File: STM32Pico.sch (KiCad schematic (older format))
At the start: 25 parts, among them J1 2.54mm header 01x20, J2 2.54mm header 01x20, SW1 Boot Mode, SW2 Reset Switch, U1 STM32F411CEUx, U2 XC6206PxxxMR, X1 ECS-2520MV-xxx-xx

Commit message: finished up board design, likely needs some check overs and revision.
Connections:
- net GND: now also U1.23 (VSS), U1.35 (VSS), U1.47 (VSS)
- net PA0: now also J1.4 (Pin_4)
- net PA1: now also J1.2 (Pin_2)
- net PA10: now also J2.6 (Pin_6)
- net PA13: now also J1.20 (Pin_20)
- net PA14: now also J1.19 (Pin_19)
- net PA15: now also J1.17 (Pin_17)
- net PA2: now also J1.1 (Pin_1)
- net PA7: now also J2.20 (Pin_20)
- net PA8: now also J2.9 (Pin_9)
- net PA9: now also J2.7 (Pin_7)
- net PB0: now also J2.19 (Pin_19)
- net PB1: now also J2.17 (Pin_17)
- net PB10: now also J2.15 (Pin_15)
- net PB12: now also J2.14 (Pin_14)
- net PB13: now also J2.12 (Pin_12)
- net PB14: now also J2.11 (Pin_11)
- net PB15: now also J2.10 (Pin_10)
- net PB2: now also J2.16 (Pin_16)
- net PB3: now also J1.16 (Pin_16)
- net PB4: now also J1.15 (Pin_15)
- net PB5: now also J1.14 (Pin_14)
- net PB6: now also J1.12 (Pin_12)
- net PB7: now also J1.11 (Pin_11)
- net PB8: now also J1.10 (Pin_10)
- net PB9: now also J1.9 (Pin_9)
- net PC15: now reaches J1.5 (Pin_5)
- net PC15: now also U1.4 (PC15)
- net PC14: now reaches J1.6 (Pin_6)
- net PC14: now also U1.3 (PC14)
- net PC13: now reaches J1.7 (Pin_7)
- net PC13: now also U1.2 (PC13)
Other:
- moved on the sheet: J1, J2

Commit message: properly seperated VBUS and VSYS however VSYS is now 5V output only since its not connected to the power management IC
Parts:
- D1: value Schottky 0603 -> 1N4002 0603; symbol Device:D_Schottky -> Device:D
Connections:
- net VBUS: no longer D1.1 (K), J2.2 (Pin_2)
- new net VSYS: D1.1 (K), J2.2 (Pin_2)
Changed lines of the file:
@@
-$EndComp
-$Comp
-L power:VBUS #PWR016
-U 1 1 615E9702
-P 3200 1500
-F 0 "#PWR016" H 3200 1350 50  0001 C CNN
-F 1 "VBUS" V 3215 1627 50  0000 L CNN
-F 2 "" H 3200 1500 50  0001 C CNN
-F 3 "" H 3200 1500 50  0001 C CNN
-	1    3200 1500
-	0    -1   -1   0
 $EndComp
 $Comp
@@
 	6150 7250 6450 7250
 $Comp
-L Device:D_Schottky D1
+L Device:D D1
 U 1 1 611CF5D5
 P 3350 1500
 F 0 "D1" H 3350 1331 50  0000 C CNN
-F 1 "Schottky 0603" H 3350 1398 20  0000 C CNN
+F 1 "1N4002 0603" H 3350 1398 20  0000 C CNN
 F 2 "Diode_SMD:D_0603_1608Metric" H 3350 1500 50  0001 C CNN
 F 3 "~" H 3350 1500 50  0001 C CNN
@@
 	3650 1950 3800 1950
 Connection ~ 3800 1950
-$Comp
-L VSYS:VSYS #PWR0101
-U 1 1 610575B5
-P 3650 1950
-F 0 "#PWR0101" H 3650 1800 50  0001 C CNN
-F 1 "VSYS" V 3665 2077 50  0000 L CNN
-F 2 "" H 3650 1950 50  0001 C CNN
-F 3 "" H 3650 1950 50  0001 C CNN
-	1    3650 1950
-	0    -1   -1   0
-$EndComp
-$Comp
-L VSYS:VSYS #PWR0102
-U 1 1 61057CA3
-P 3500 1500
-F 0 "#PWR0102" H 3500 1350 50  0001 C CNN
-F 1 "VSYS" V 3515 1628 50  0000 L CNN
-F 2 "" H 3500 1500 50  0001 C CNN
-F 3 "" H 3500 1500 50  0001 C CNN
-	1    3500 1500
-	0    1    1    0
-$EndComp
-$Comp
-L VSYS:VSYS #PWR0103
-U 1 1 61058306
-P 6400 7050
-F 0 "#PWR0103" H 6400 6900 50  0001 C CNN
-F 1 "VSYS" V 6415 7177 50  0000 L CNN
-F 2 "" H 6400 7050 50  0001 C CNN
-F 3 "" H 6400 7050 50  0001 C CNN
-	1    6400 7050
-	0    -1   -1   0
-$EndComp
 Text GLabel 2200 8550 0    50   Input ~ 0
 PB0
@@
 Text GLabel 6450 8850 0    50   Input ~ 0
 PA7
+$Comp
+L power:VBUS #PWR016
+U 1 1 615E9702
+P 3200 1500
+F 0 "#PWR016" H 3200 1350 50  0001 C CNN
+F 1 "VBUS" V 3215 1627 50  0000 L CNN
+F 2 "" H 3200 1500 50  0001 C CNN
+F 3 "" H 3200 1500 50  0001 C CNN
+	1    3200 1500
+	0    -1   -1   0
+$EndComp
+Text GLabel 3500 1500 2    50   Input ~ 0
+VSYS
+$Comp
+L power:VBUS #PWR?
+U 1 1 6117FC90
+P 3650 1950
+F 0 "#PWR?" H 3650 1800 50  0001 C CNN
+F 1 "VBUS" V 3665 2077 50  0000 L CNN
+F 2 "" H 3650 1950 50  0001 C CNN
+F 3 "" H 3650 1950 50  0001 C CNN
+	1    3650 1950
+	0    -1   -1   0
+$EndComp
+Text GLabel 6400 7050 0    50   Input ~ 0
+VSYS
 $EndSCHEMATC

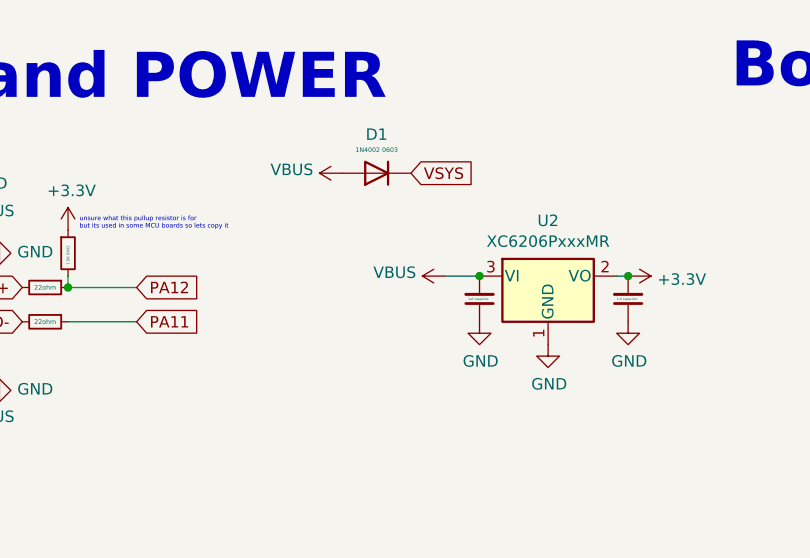
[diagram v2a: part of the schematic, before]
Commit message: changed my mind - moved power ic to vsys and also adjusted USB traces to correct some phase skew.
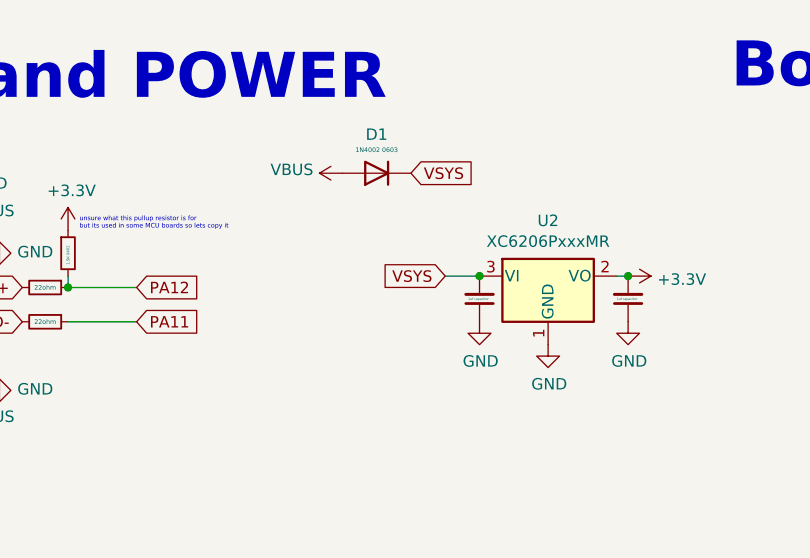
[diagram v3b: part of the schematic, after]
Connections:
- net VBUS: no longer C6.2, U2.3 (VI)
- net VSYS: now also C6.2, U2.3 (VI)
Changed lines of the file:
@@
 Text GLabel 3500 1500 2    50   Input ~ 0
 VSYS
-$Comp
-L power:VBUS #PWR?
-U 1 1 6117FC90
-P 3650 1950
-F 0 "#PWR?" H 3650 1800 50  0001 C CNN
-F 1 "VBUS" V 3665 2077 50  0000 L CNN
-F 2 "" H 3650 1950 50  0001 C CNN
-F 3 "" H 3650 1950 50  0001 C CNN
-	1    3650 1950
-	0    -1   -1   0
-$EndComp
 Text GLabel 6400 7050 0    50   Input ~ 0
 VSYS
+Text GLabel 3650 1950 0    50   Input ~ 0
+VSYS
 $EndSCHEMATC

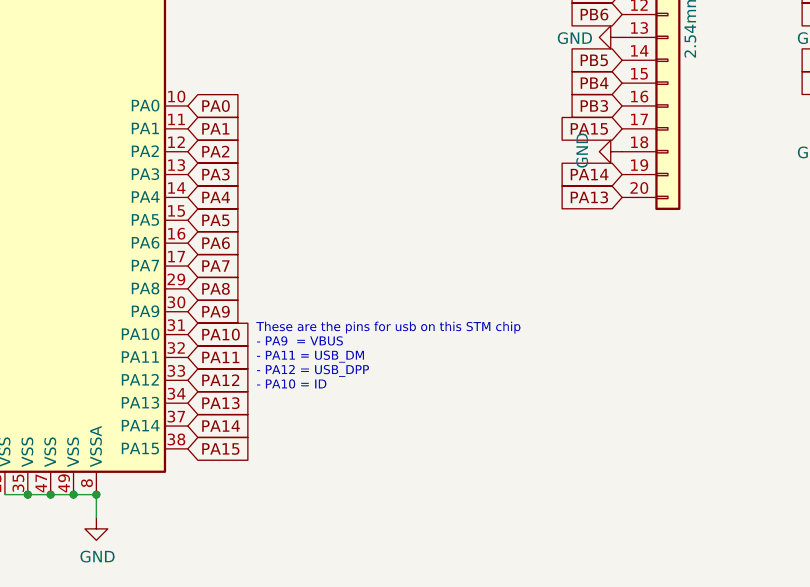
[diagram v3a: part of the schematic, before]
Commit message: added pin lables and Jtag/swdio/swclk on the PCB
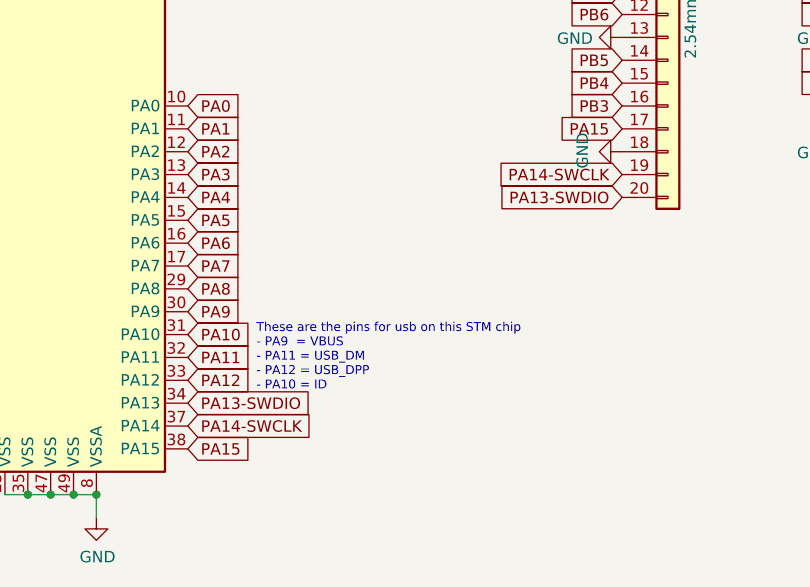
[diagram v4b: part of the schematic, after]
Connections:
- net PA13 renamed PA13-SWDIO
- net PA14 renamed PA14-SWCLK
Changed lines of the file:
@@
 PA10
 Text GLabel 3500 9750 2    50   Input ~ 0
-PA13
+PA13-SWDIO
 Text GLabel 3500 9850 2    50   Input ~ 0
-PA14
+PA14-SWCLK
 Text GLabel 3500 9950 2    50   Input ~ 0
 PA15
@@
 PA8
 Text GLabel 5400 8750 0    50   Input ~ 0
-PA14
+PA14-SWCLK
 Text GLabel 5400 8550 0    50   Input ~ 0
 PA15
@@
 Text GLabel 5400 7350 0    50   Input ~ 0
 PC15
-Text GLabel 5400 8850 0    50   Input ~ 0
-PA13
 Text GLabel 5400 7250 0    50   Input ~ 0
 PA0
@@
 Text GLabel 3650 1950 0    50   Input ~ 0
 VSYS
+Text GLabel 5400 8850 0    50   Input ~ 0
+PA13-SWDIO
 $EndSCHEMATC

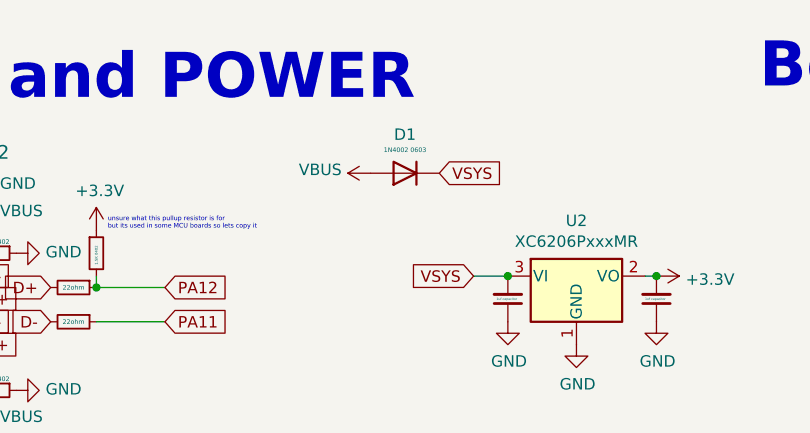
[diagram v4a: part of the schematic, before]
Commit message: changed diode for more common type
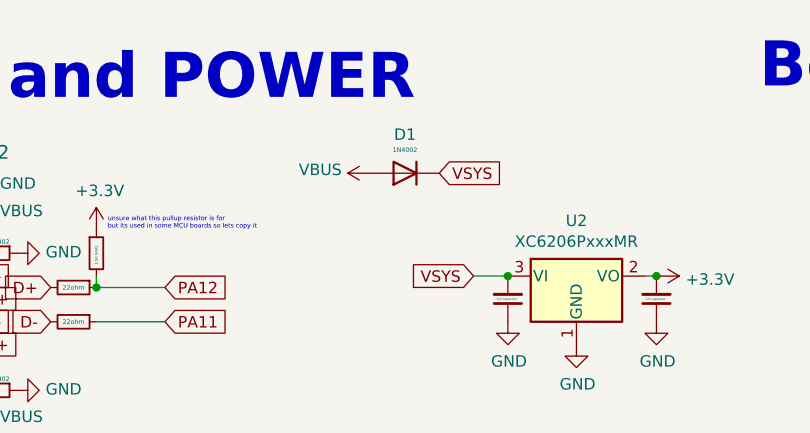
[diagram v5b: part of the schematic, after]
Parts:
- D1: value 1N4002 0603 -> 1N4002; footprint Diode_SMD:D_0603_1608Metric -> Diode_SMD:D_SOD-123
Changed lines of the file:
@@
 P 3350 1500
 F 0 "D1" H 3350 1331 50  0000 C CNN
-F 1 "1N4002 0603" H 3350 1398 20  0000 C CNN
-F 2 "Diode_SMD:D_0603_1608Metric" H 3350 1500 50  0001 C CNN
+F 1 "1N4002" H 3350 1398 20  0000 C CNN
+F 2 "Diode_SMD:D_SOD-123" H 3350 1500 50  0001 C CNN
 F 3 "~" H 3350 1500 50  0001 C CNN
 	1    3350 1500

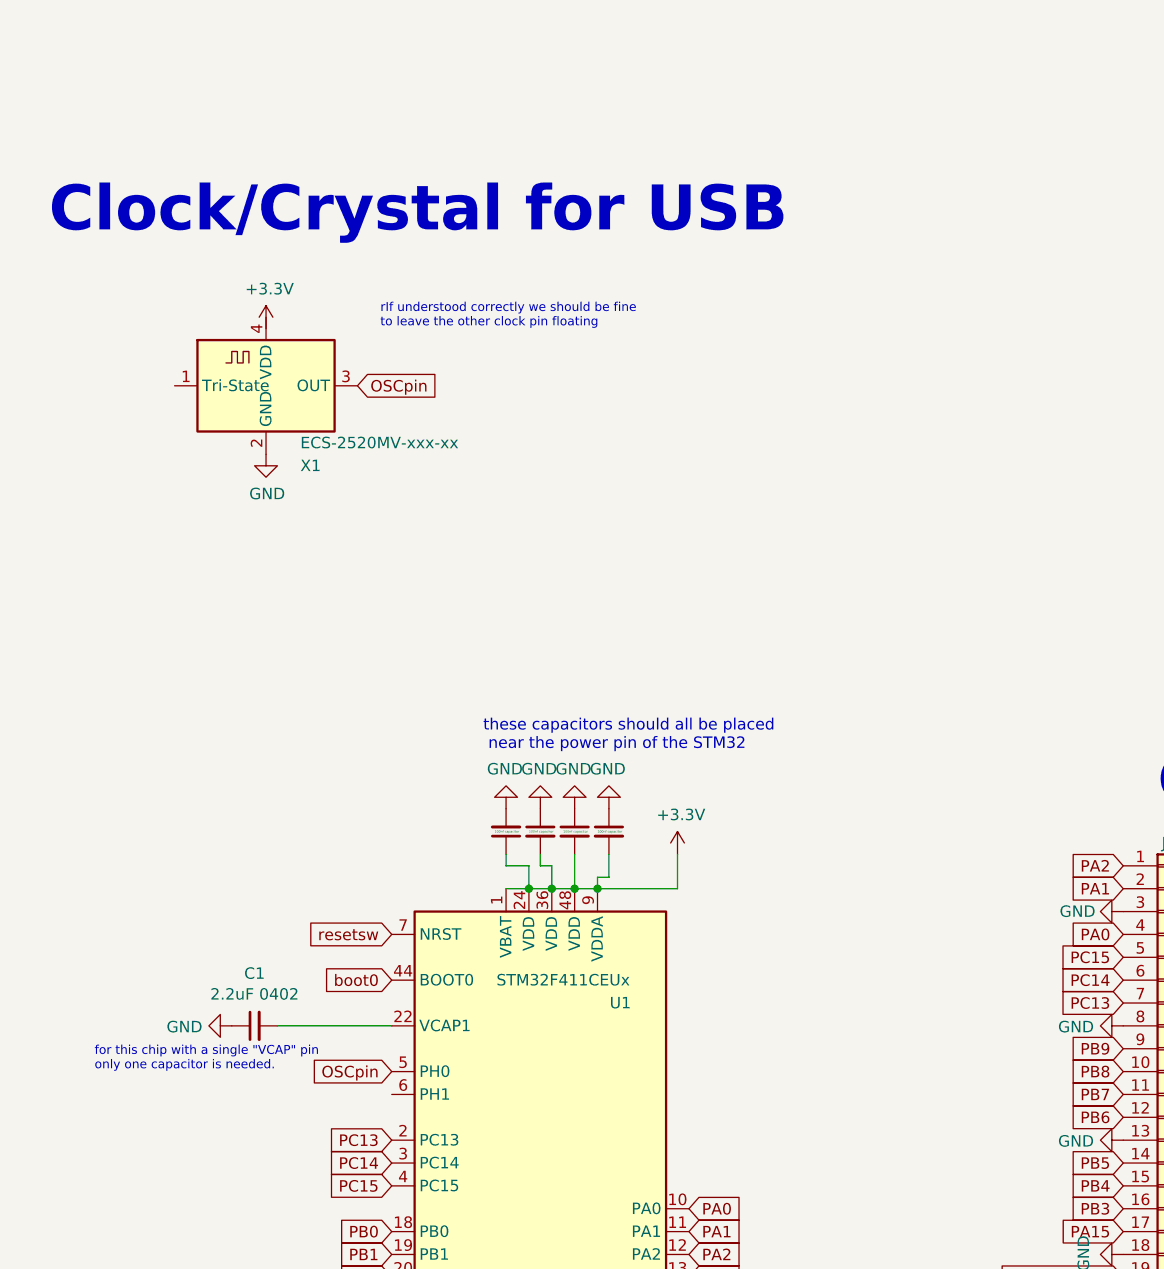
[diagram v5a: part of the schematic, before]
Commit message: swapped oscilator for crystal and adjusted various nearby parts and traces.
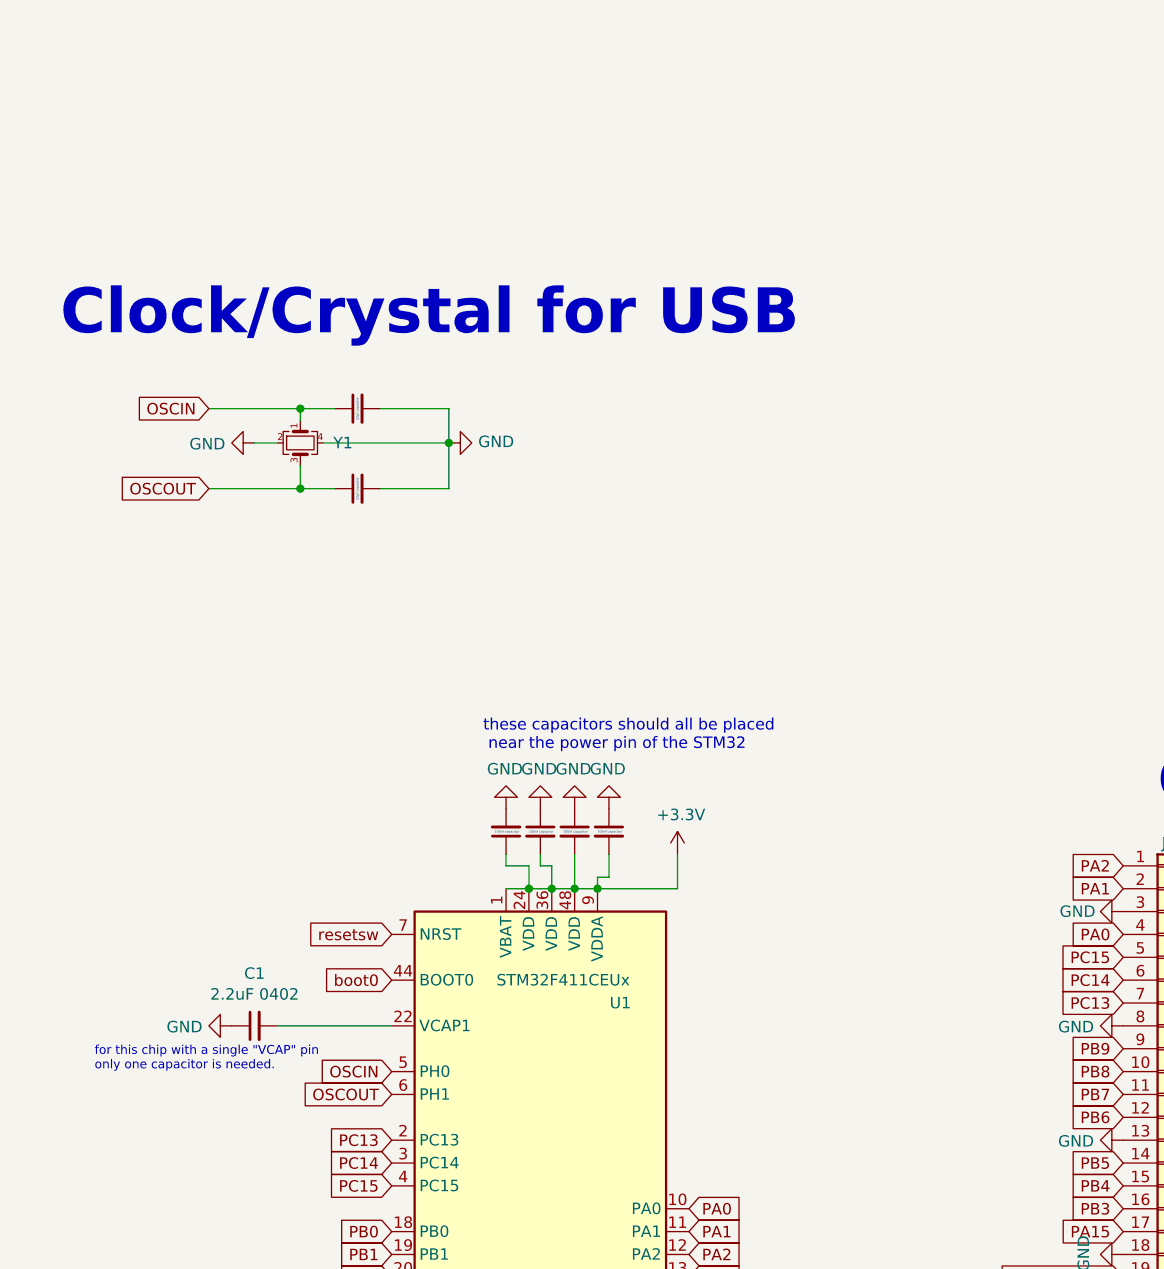
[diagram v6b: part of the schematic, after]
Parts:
- removed X1: ECS-2520MV-xxx-xx, Oscillator:Oscillator_SMD_ECS_2520MV-xxx-xx-4Pin_2.5x2.0mm, symbol Oscillator:ECS-2520MV-xxx-xx
- added C10, C11: 22pf capacitor, Capacitor_SMD:C_0402_1005Metric, symbol Device:C_Small
- added Y1: 8Mhz 3225, Crystal:Crystal_SMD_3225-4Pin_3.2x2.5mm, symbol Device:Crystal_GND24_Small
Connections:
- net GND: now also C10.2, C11.2, Y1.2, Y1.4
- net OSCOUT: now reaches U1.6 (PH1)
- net OSCOUT: now also C11.1, Y1.3
- net OSCpin renamed OSCIN
- net OSCIN: now also C10.1, Y1.1
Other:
- note removed: "rIf understood correctly we should be fine\nto leave the other clock pin floating"
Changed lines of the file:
@@
 	6150 7350 6450 7350
-$Comp
-L MCU_ST_STM32F4:STM32F411CEUx U1
-U 1 1 61118AF8
-P 2900 8550
-F 0 "U1" H 3200 9550 50  0000 C CNN
-F 1 "STM32F411CEUx" H 2950 9650 50  0000 C CNN
-F 2 "Package_DFN_QFN:QFN-48-1EP_7x7mm_P0.5mm_EP5.6x5.6mm" H 2300 7050 50  0001 R CNN
-F 3 "http://www.st.com/st-web-ui/static/active/en/resource/technical/document/datasheet/DM00115249.pdf" H 2900 8550 50  0001 C CNN
-	1    2900 8550
-	1    0    0    -1
-$EndComp
 $Comp
 L Regulator_Linear:XC6206PxxxMR U2
@@
 	1    0    0    -1
 $EndComp
-$Comp
-L Oscillator:ECS-2520MV-xxx-xx X1
-U 1 1 60E5B405
-P 1650 4850
-F 0 "X1" H 1800 4500 50  0000 L CNN
-F 1 "ECS-2520MV-xxx-xx" H 1800 4600 50  0000 L CNN
-F 2 "Oscillator:Oscillator_SMD_ECS_2520MV-xxx-xx-4Pin_2.5x2.0mm" H 2100 4500 50  0001 C CNN
-F 3 "https://www.ecsxtal.com/store/pdf/ECS-2520MV.pdf" H 1475 4975 50  0001 C CNN
-	1    1650 4850
-	1    0    0    -1
-$EndComp
-Text GLabel 2050 4850 2    50   Input ~ 0
-OSCpin
 Text GLabel 2200 7850 0    50   Input ~ 0
-OSCpin
-$Comp
-L power:+3.3V #PWR08
-U 1 1 60E980B3
-P 1650 4600
-F 0 "#PWR08" H 1650 4450 50  0001 C CNN
-F 1 "+3.3V" H 1665 4773 50  0000 C CNN
-F 2 "" H 1650 4600 50  0001 C CNN
-F 3 "" H 1650 4600 50  0001 C CNN
-	1    1650 4600
-	1    0    0    -1
-$EndComp
-$Comp
-L power:GND #PWR09
-U 1 1 60E99EB6
-P 1650 5150
-F 0 "#PWR09" H 1650 4900 50  0001 C CNN
-F 1 "GND" H 1655 4977 50  0000 C CNN
-F 2 "" H 1650 5150 50  0001 C CNN
-F 3 "" H 1650 5150 50  0001 C CNN
-	1    1650 5150
-	1    0    0    -1
-$EndComp
+OSCIN
 Text GLabel 2200 7450 0    50   Input ~ 0
 boot0
@@
 $EndComp
 Wire Wire Line
-	3000 10150 3100 10150
-Wire Wire Line
 	3000 6900 3000 7050
 Connection ~ 2800 7050
-Connection ~ 3100 10150
 Text Notes 900  1200 0    197  ~ 39
 USB and POWER
-Text Notes 700  4200 0    197  ~ 39
+Text Notes 750  4650 0    197  ~ 39
 Clock/Crystal for USB
 $Comp
@@
 	-1   0    0    1
 $EndComp
-Text Notes 2150 4600 0    39   ~ 0
-rIf understood correctly we should be fine\nto leave the other clock pin floating
 Text Notes 3800 9700 0    39   ~ 0
 These are the pins for usb on this STM chip\n- PA9  = VBUS\n- PA11 = USB_DM\n- PA12 = USB_DPP\n- PA10 = ID
@@
 Text GLabel 5400 7750 0    50   Input ~ 0
 PB9
-Wire Wire Line
-	2700 10150 2800 10150
-Connection ~ 3000 10150
-Connection ~ 2800 10150
-Wire Wire Line
-	2800 10150 2900 10150
-Connection ~ 2900 10150
-Wire Wire Line
-	2900 10150 3000 10150
 Text GLabel 2200 8150 0    50   Input ~ 0
 PC13
@@
 Text GLabel 5400 8850 0    50   Input ~ 0
 PA13-SWDIO
+Connection ~ 2900 10150
+Connection ~ 2800 10150
+Connection ~ 3000 10150
+Wire Wire Line
+	2800 10150 2900 10150
+Wire Wire Line
+	2700 10150 2800 10150
+Connection ~ 3100 10150
+Wire Wire Line
+	2900 10150 3000 10150
+Wire Wire Line
+	3000 10150 3100 10150
+$Comp
+L MCU_ST_STM32F4:STM32F411CEUx U1
+U 1 1 61118AF8
+P 2900 8550
+F 0 "U1" H 3200 9550 50  0000 C CNN
+F 1 "STM32F411CEUx" H 2950 9650 50  0000 C CNN
+F 2 "Package_DFN_QFN:QFN-48-1EP_7x7mm_P0.5mm_EP5.6x5.6mm" H 2300 7050 50  0001 R CNN
+F 3 "http://www.st.com/st-web-ui/static/active/en/resource/technical/document/datasheet/DM00115249.pdf" H 2900 8550 50  0001 C CNN
+	1    2900 8550
+	1    0    0    -1
+$EndComp
+Text GLabel 2200 7950 0    50   Input ~ 0
+OSCOUT
+Text GLabel 1400 5300 0    50   Input ~ 0
+OSCOUT
+Text GLabel 1400 4950 0    50   Input ~ 0
+OSCIN
+$Comp
+L Device:C_Small C10
+U 1 1 6193F656
+P 2050 4950
+F 0 "C10" H 2142 4996 50  0001 L CNN
+F 1 "22pf capacitor" H 2000 4950 10  0000 L CNN
+F 2 "Capacitor_SMD:C_0402_1005Metric" H 2050 4950 50  0001 C CNN
+F 3 "~" H 2050 4950 50  0001 C CNN
+	1    2050 4950
+	0    -1   1    0
+$EndComp
+$Comp
+L Device:C_Small C11
+U 1 1 6193FD78
+P 2050 5300
+F 0 "C11" H 2142 5346 50  0001 L CNN
+F 1 "22pf capacitor" H 2000 5300 10  0000 L CNN
+F 2 "Capacitor_SMD:C_0402_1005Metric" H 2050 5300 50  0001 C CNN
+F 3 "~" H 2050 5300 50  0001 C CNN
+	1    2050 5300
+	0    -1   1    0
+$EndComp
+Wire Wire Line
+	2150 4950 2450 4950
+Wire Wire Line
+	2450 4950 2450 5100
+Wire Wire Line
+	2450 5300 2450 5100
+Connection ~ 2450 5100
+Wire Wire Line
+	2150 5300 2450 5300
+$Comp
+L Device:Crystal_GND24_Small Y1
+U 1 1 61944889
+P 1800 5100
+F 0 "Y1" V 1800 5244 50  0000 L CNN
+F 1 "8Mhz 3225" V 1845 5244 50  0001 L CNN
+F 2 "Crystal:Crystal_SMD_3225-4Pin_3.2x2.5mm" H 1800 5100 50  0001 C CNN
+F 3 "~" H 1800 5100 50  0001 C CNN
+	1    1800 5100
+	0    1    1    0
+$EndComp
+Wire Wire Line
+	1800 5000 1800 4950
+Wire Wire Line
+	1800 4950 1950 4950
+Wire Wire Line
+	1800 4950 1400 4950
+Connection ~ 1800 4950
+Wire Wire Line
+	1400 5300 1800 5300
+Wire Wire Line
+	1800 5200 1800 5300
+Connection ~ 1800 5300
+Wire Wire Line
+	1800 5300 1950 5300
+$Comp
+L power:GND #PWR0102
+U 1 1 6194B002
+P 2450 5100
+F 0 "#PWR0102" H 2450 4850 50  0001 C CNN
+F 1 "GND" V 2455 4972 50  0000 R CNN
+F 2 "" H 2450 5100 50  0001 C CNN
+F 3 "" H 2450 5100 50  0001 C CNN
+	1    2450 5100
+	0    -1   -1   0
+$EndComp
+Wire Wire Line
+	1900 5100 2450 5100
+$Comp
+L power:GND #PWR?
+U 1 1 6195625B
+P 1600 5100
+F 0 "#PWR?" H 1600 4850 50  0001 C CNN
+F 1 "GND" V 1605 4972 50  0000 R CNN
+F 2 "" H 1600 5100 50  0001 C CNN
+F 3 "" H 1600 5100 50  0001 C CNN
+	1    1600 5100
+	0    1    1    0
+$EndComp
+Wire Wire Line
+	1600 5100 1700 5100
 $EndSCHEMATC
